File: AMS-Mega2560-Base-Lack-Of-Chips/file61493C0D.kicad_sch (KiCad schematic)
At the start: 50 parts, among them IC10 LM2597MX-ADJ_NOPB, IC11 LM2597M-3.3_NOPB, IC12 OPA2340PA, IC9 LM2670SX-5.0_NOPB, J21 Screw_Terminal_01x03, J22 Conn_01x07, Q21 IRF9Z34NPBF, Q22 IRF9610PBF-BE3, Q23 2N7000, Q5 2N7000, Q6 IRF9Z34NPBF, U1 BK_HTC-15M, U2 TL431LP

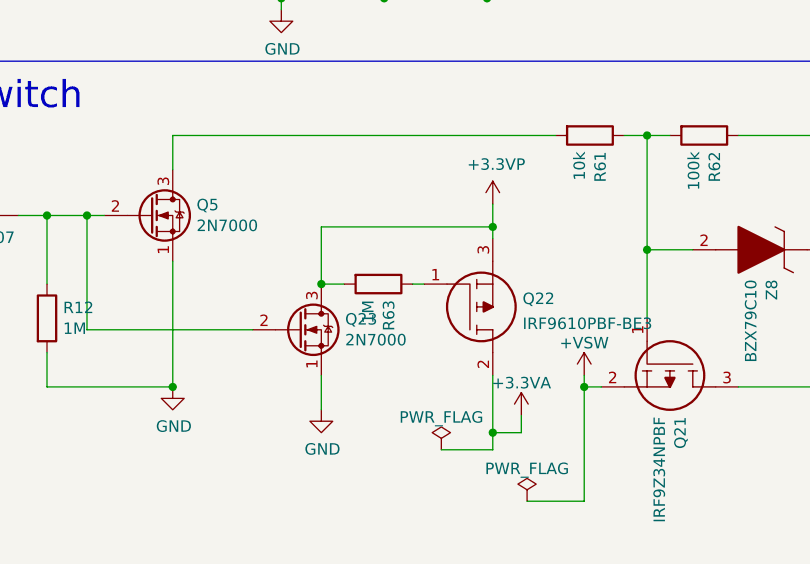
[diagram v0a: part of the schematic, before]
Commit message: updating some Resistor values
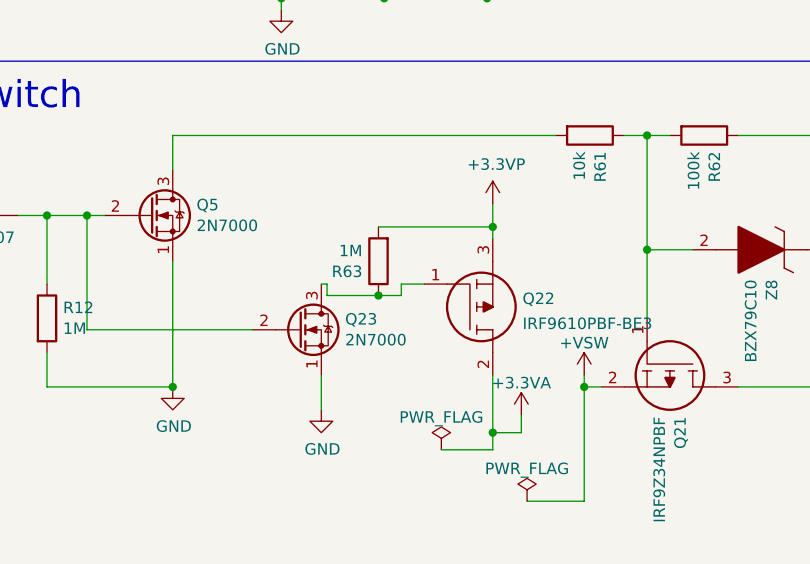
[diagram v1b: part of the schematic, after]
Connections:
- net +3.3VP: no longer Q23.3 (D)
- net at Q22.1, R63.1: now also Q23.3 (D)
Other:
- moved on the sheet: R63
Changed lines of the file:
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@@
   (junction (at 167.64 82.55) (diameter 0) (color 0 0 0 0)
   )
+  (junction (at 71.755 182.245) (diameter 0) (color 0 0 0 0)
+  )
   (junction (at 267.97 69.85) (diameter 0) (color 0 0 0 0)
   )
   (junction (at 48.895 192.405) (diameter 0) (color 0 0 0 0)
-  )
-  (junction (at 65.405 180.975) (diameter 0) (color 0 0 0 0)
   )
   (junction (at 207.01 67.31) (diameter 0) (color 0 0 0 0)
@@
     (stroke (width 0) (type default) (color 0 0 0 0))
   )
+  (wire (pts (xy 74.295 182.245) (xy 71.755 182.245))
+    (stroke (width 0) (type default) (color 0 0 0 0))
+  )
   (wire (pts (xy 99.06 126.365) (xy 99.06 125.095))
     (stroke (width 0) (type default) (color 0 0 0 0))
@@
     (stroke (width 0) (type default) (color 0 0 0 0))
   )
+  (wire (pts (xy 74.295 180.975) (xy 74.295 182.245))
+    (stroke (width 0) (type default) (color 0 0 0 0))
+  )
   (wire (pts (xy 84.455 191.135) (xy 84.455 197.485))
     (stroke (width 0) (type default) (color 0 0 0 0))
@@
     (stroke (width 0) (type default) (color 0 0 0 0))
   )
-  (wire (pts (xy 65.405 180.975) (xy 65.405 174.625))
-    (stroke (width 0) (type default) (color 0 0 0 0))
-  )
   (wire (pts (xy 77.47 63.5) (xy 77.47 62.23))
     (stroke (width 0) (type default) (color 0 0 0 0))
@@
     (stroke (width 0) (type default) (color 0 0 0 0))
   )
+  (wire (pts (xy 71.755 174.625) (xy 84.455 174.625))
+    (stroke (width 0) (type default) (color 0 0 0 0))
+  )
   (wire (pts (xy 167.64 63.5) (xy 167.64 58.42))
     (stroke (width 0) (type default) (color 0 0 0 0))
@@
     (stroke (width 0) (type default) (color 0 0 0 0))
   )
+  (wire (pts (xy 66.04 180.975) (xy 65.405 180.975))
+    (stroke (width 0) (type default) (color 0 0 0 0))
+  )
   (wire (pts (xy 241.3 125.73) (xy 241.3 142.24))
     (stroke (width 0) (type default) (color 0 0 0 0))
@@
     (stroke (width 0) (type default) (color 0 0 0 0))
   )
-  (wire (pts (xy 65.405 174.625) (xy 84.455 174.625))
-    (stroke (width 0) (type default) (color 0 0 0 0))
-  )
   (wire (pts (xy 273.05 47.625) (xy 273.05 43.18))
     (stroke (width 0) (type default) (color 0 0 0 0))
@@
     (stroke (width 0) (type default) (color 0 0 0 0))
   )
-  (wire (pts (xy 67.945 180.975) (xy 65.405 180.975))
-    (stroke (width 0) (type default) (color 0 0 0 0))
-  )
   (wire (pts (xy 102.87 54.61) (xy 95.25 54.61))
     (stroke (width 0) (type default) (color 0 0 0 0))
@@
     (stroke (width 0) (type default) (color 0 0 0 0))
   )
-  (wire (pts (xy 75.565 180.975) (xy 76.835 180.975))
+  (wire (pts (xy 66.04 182.245) (xy 66.04 180.975))
+    (stroke (width 0) (type default) (color 0 0 0 0))
+  )
+  (wire (pts (xy 74.295 180.975) (xy 76.835 180.975))
     (stroke (width 0) (type default) (color 0 0 0 0))
   )
@@
   )
   (wire (pts (xy 172.72 82.55) (xy 179.07 82.55))
+    (stroke (width 0) (type default) (color 0 0 0 0))
+  )
+  (wire (pts (xy 71.755 182.245) (xy 66.04 182.245))
     (stroke (width 0) (type default) (color 0 0 0 0))
   )
@@
     (pin "3")
   )
-  (symbol (lib_id "Device:R") (at 71.755 180.975 270) (unit 1)
-    (in_bom yes) (on_board yes)
-    (property "Reference" "R63" (id 0) (at 72.9234 182.753 0)
-      (effects (font (size 1.27 1.27)) (justify left))
-    )
-    (property "Value" "1M" (id 1) (at 70.612 182.753 0)
-      (effects (font (size 1.27 1.27)) (justify left))
-    )
-    (property "Footprint" "Resistor_THT:R_Axial_DIN0207_L6.3mm_D2.5mm_P2.54mm_Vertical" (id 2) (at 71.755 179.197 90)
-      (effects (font (size 1.27 1.27)) hide)
-    )
-    (property "Datasheet" "~" (id 3) (at 71.755 180.975 0)
-      (effects (font (size 1.27 1.27)) hide)
-    )
+  (symbol (lib_id "Device:R") (at 71.755 178.435 180) (unit 1)
+    (in_bom yes) (on_board yes)
+    (property "Reference" "R63" (id 0) (at 69.977 179.6034 0)
+      (effects (font (size 1.27 1.27)) (justify left))
+    )
+    (property "Value" "1M" (id 1) (at 69.977 177.292 0)
+      (effects (font (size 1.27 1.27)) (justify left))
+    )
+    (property "Footprint" "Resistor_THT:R_Axial_DIN0207_L6.3mm_D2.5mm_P2.54mm_Vertical" (id 2) (at 73.533 178.435 90)
+      (effects (font (size 1.27 1.27)) hide)
+    )
+    (property "Datasheet" "~" (id 3) (at 71.755 178.435 0)
+      (effects (font (size 1.27 1.27)) hide)
+    )
